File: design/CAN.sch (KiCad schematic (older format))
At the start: 4 parts, among them U401 SN65HVD232

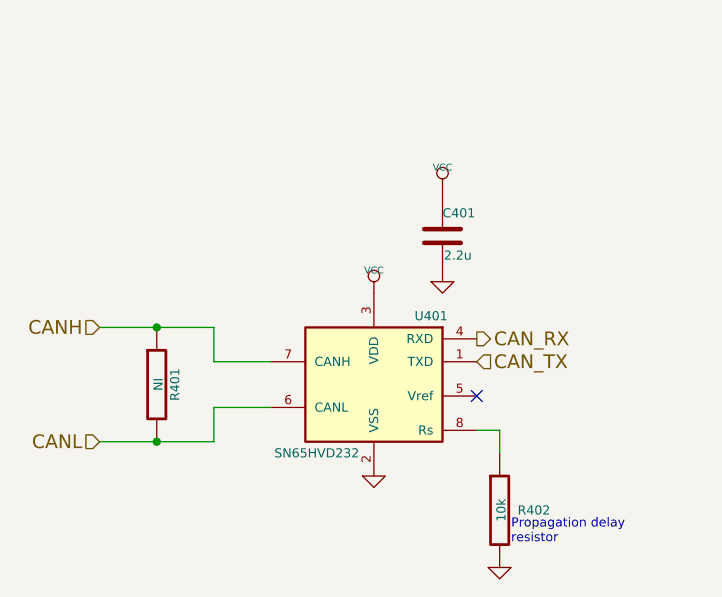
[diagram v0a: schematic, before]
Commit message: Implemented some improvements in schematic, but layout is completely new.
Changes in schematic:
- 3.3V or 5V CAN transceiver can be used
- DRV8301 can also be used and configured via SPI
- JTAG connector changed
- Fixed pinning of P1
- Some additional decoupling and/or filtering of analog signals
- Improved buck design according TI Webench recommendation
- Changed some component values
- maybe others...

Changes in layout:
- completely new layout
- placement of the big components is unchanged
- CAN connector rotated by 180°
- kept one layer free as a good GND plane
- many traces should be shorter and have lower impedance now
- improved buck layout

Other changes:
- updated gerber files
- updated PDFs (schematic and component placement)
- deleted all outdated files except libraries and datasheets
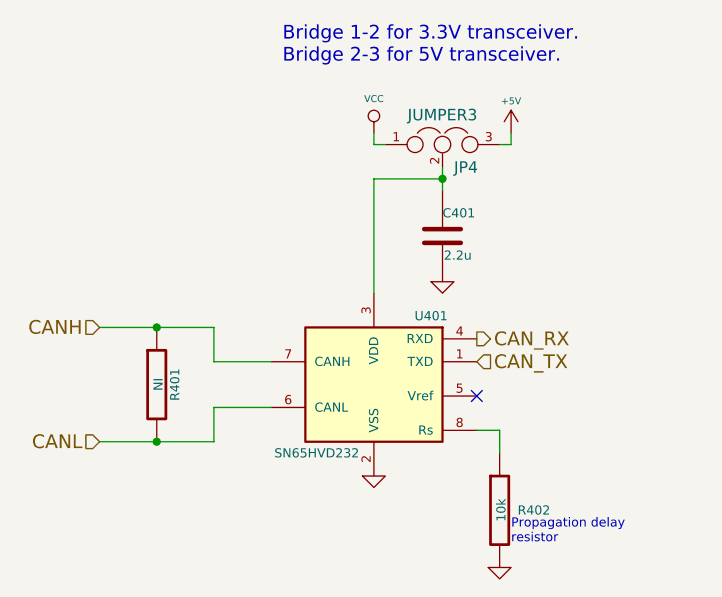
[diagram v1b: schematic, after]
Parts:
- added JP4: JUMPER3, open-project:S_JUMPER_3, symbol JUMPER3
- C401: Part# (none) -> GRM188R61C225KAAD or GRM188C81A225KAAD
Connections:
- net VCC: now also JP4.1; no longer C401.1, U401.3 (VDD)
- new net: C401.1, JP4.2, U401.3 (VDD)
- new net +5V: JP4.3
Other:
- note added: "Bridge 1-2 for 3.3V transceiver.\nBridge 2-3 for 5V transceiver."
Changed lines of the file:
@@
 EESchema Schematic File Version 2
-LIBS:BLDC_4-rescue
 LIBS:power
 LIBS:device
@@
 LIBS:contrib
 LIBS:valves
-LIBS:crf_1
 LIBS:BLDC_4-cache
 EELAYER 25 0
@@
 encoding utf-8
 Sheet 4 7
-Title "BLDC Driver 4.11"
-Date "21 aug 2015"
-Rev "4.11"
+Title "BLDC Driver 4.11p"
+Date "2016-01-06"
+Rev "A"
 Comp "Benjamin Vedder"
-Comment1 ""
+Comment1 "modified by pikim"
 Comment2 ""
 Comment3 ""
@@
 $EndComp
 $Comp
-L VCC #PWR026
-U 1 1 53F59F9D
-P 5850 3650
-F 0 "#PWR026" H 5850 3750 30  0001 C CNN
-F 1 "VCC" H 5850 3750 30  0000 C CNN
-F 2 "" H 5850 3650 60  0001 C CNN
-F 3 "" H 5850 3650 60  0001 C CNN
-	1    5850 3650
-	1    0    0    -1
-$EndComp
-$Comp
 L C-RESCUE-BLDC_4 C401
 U 1 1 53F59FA3
@@
 F 2 "CRF1:SMD-0603_c" H 6188 3250 30  0001 C CNN
 F 3 "" H 6150 3400 60  0000 C CNN
+F 4 "GRM188R61C225KAAD or GRM188C81A225KAAD" H 6150 3400 60  0001 C CNN "Part#"
 	1    6150 3400
 	1    0    0    -1
 $EndComp
 $Comp
-L VCC #PWR027
-U 1 1 53F59FAA
-P 6150 3200
-F 0 "#PWR027" H 6150 3300 30  0001 C CNN
-F 1 "VCC" H 6150 3300 30  0000 C CNN
-F 2 "" H 6150 3200 60  0001 C CNN
-F 3 "" H 6150 3200 60  0001 C CNN
-	1    6150 3200
-	1    0    0    -1
-$EndComp
-$Comp
-L GND-RESCUE-BLDC_4 #PWR028
+L GND-RESCUE-BLDC_4 #PWR026
 U 1 1 53F59FB0
 P 6150 3600
-F 0 "#PWR028" H 6150 3600 30  0001 C CNN
+F 0 "#PWR026" H 6150 3600 30  0001 C CNN
 F 1 "GND" H 6150 3530 30  0001 C CNN
 F 2 "" H 6150 3600 60  0000 C CNN
@@
 Text HLabel 4650 4300 0    60   Input ~ 0
 CANL
-Wire Wire Line
-	4650 4300 5150 4300
-Wire Wire Line
-	5150 4300 5150 4150
-Wire Wire Line
-	5150 4150 5400 4150
-Connection ~ 4900 4300
-Wire Wire Line
-	5400 3950 5150 3950
-Wire Wire Line
-	5150 3950 5150 3800
-Wire Wire Line
-	5150 3800 4650 3800
-Connection ~ 4900 3800
 NoConn ~ 6300 4100
 $Comp
@@
 	1    0    0    -1
 $EndComp
-Wire Wire Line
-	6400 4350 6400 4250
-Wire Wire Line
-	6400 4250 6300 4250
 $Comp
-L GND-RESCUE-BLDC_4 #PWR029
+L GND-RESCUE-BLDC_4 #PWR027
 U 1 1 5400318B
 P 6400 4850
-F 0 "#PWR029" H 6400 4850 30  0001 C CNN
+F 0 "#PWR027" H 6400 4850 30  0001 C CNN
 F 1 "GND" H 6400 4780 30  0001 C CNN
 F 2 "" H 6400 4850 60  0000 C CNN
@@
 Text Notes 6450 4750 0    40   ~ 0
 Propagation delay\nresistor
+$Comp
+L VCC #PWR028
+U 1 1 53F59FAA
+P 5850 2950
+F 0 "#PWR028" H 5850 3050 30  0001 C CNN
+F 1 "VCC" H 5850 3100 30  0000 C CNN
+F 2 "" H 5850 2950 60  0001 C CNN
+F 3 "" H 5850 2950 60  0001 C CNN
+	1    5850 2950
+	1    0    0    -1
+$EndComp
+$Comp
+L +5V #PWR029
+U 1 1 567FBB5B
+P 6450 2950
+F 0 "#PWR029" H 6450 2800 50  0001 C CNN
+F 1 "+5V" H 6450 3090 30  0000 C CNN
+F 2 "" H 6450 2950 50  0000 C CNN
+F 3 "" H 6450 2950 50  0000 C CNN
+	1    6450 2950
+	1    0    0    -1
+$EndComp
+$Comp
+L JUMPER3 JP4
+U 1 1 567FDE17
+P 6150 3000
+F 0 "JP4" H 6200 2900 50  0000 L CNN
+F 1 "JUMPER3" H 6150 3100 50  0000 C BNN
+F 2 "open-project:S_JUMPER_3" H 6150 3000 50  0001 C CNN
+F 3 "" H 6150 3000 50  0000 C CNN
+	1    6150 3000
+	1    0    0    -1
+$EndComp
+Wire Wire Line
+	5850 3150 5850 3650
+Wire Wire Line
+	6150 3150 5850 3150
+Wire Wire Line
+	6150 3100 6150 3200
+Wire Wire Line
+	6400 4250 6300 4250
+Wire Wire Line
+	6400 4350 6400 4250
+Connection ~ 4900 3800
+Wire Wire Line
+	5150 3800 4650 3800
+Wire Wire Line
+	5150 3950 5150 3800
+Wire Wire Line
+	5400 3950 5150 3950
+Connection ~ 4900 4300
+Wire Wire Line
+	5150 4150 5400 4150
+Wire Wire Line
+	5150 4300 5150 4150
+Wire Wire Line
+	4650 4300 5150 4300
+Connection ~ 6150 3150
+Wire Wire Line
+	5850 2950 5850 3000
+Wire Wire Line
+	5850 3000 5900 3000
+Wire Wire Line
+	6400 3000 6450 3000
+Wire Wire Line
+	6450 3000 6450 2950
+Text Notes 5450 2650 0    60   ~ 0
+Bridge 1-2 for 3.3V transceiver.\nBridge 2-3 for 5V transceiver.
 $EndSCHEMATC
